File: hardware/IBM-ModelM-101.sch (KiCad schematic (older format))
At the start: 40 parts, among them J1 CONN-MOLEX-0670688000-USB-B, J2 KEYBOARD_ACTIVE_LINES, J3 KEYBOARD_INPUT_LINES, J4 CHASSIS_GROUND, J5 STATUS_LEDS, J6 DEBUG_FTDI, J7 JTAG, SW1 BOOT0, SW2 RESET, U1 TLV70233DBV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

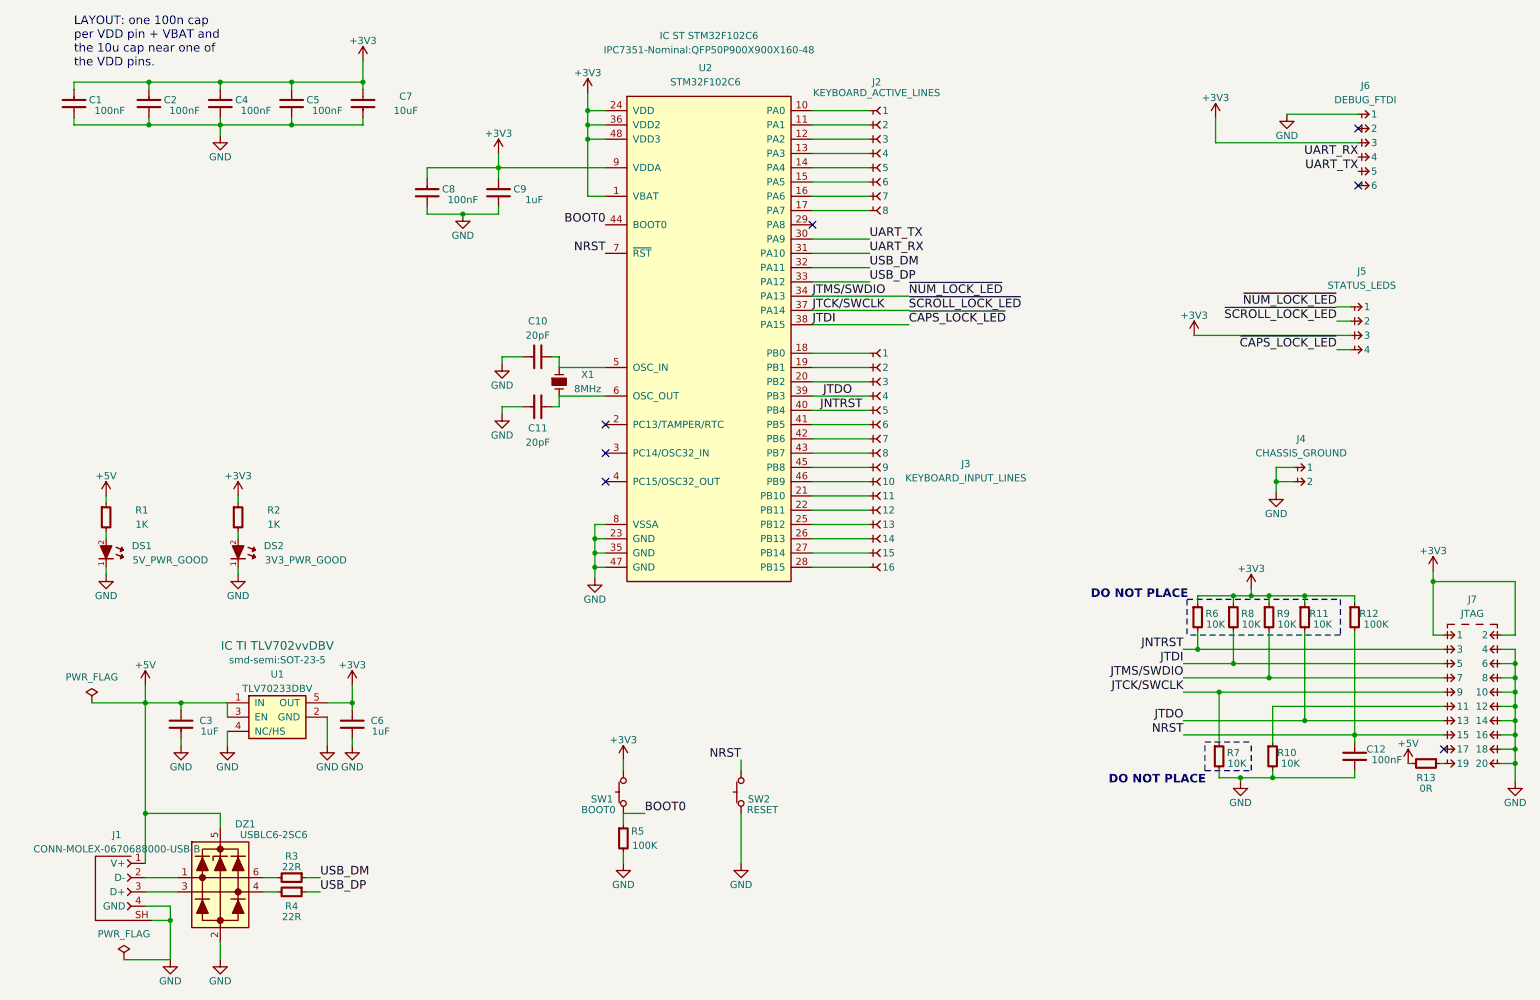
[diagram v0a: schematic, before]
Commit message: Most keys, locks working
All alpha-numerics working along with Scroll, Num andCaps lock keys.
Shift, Alt and Ctrl not working. Enter key seems to have a bug with it
as well.
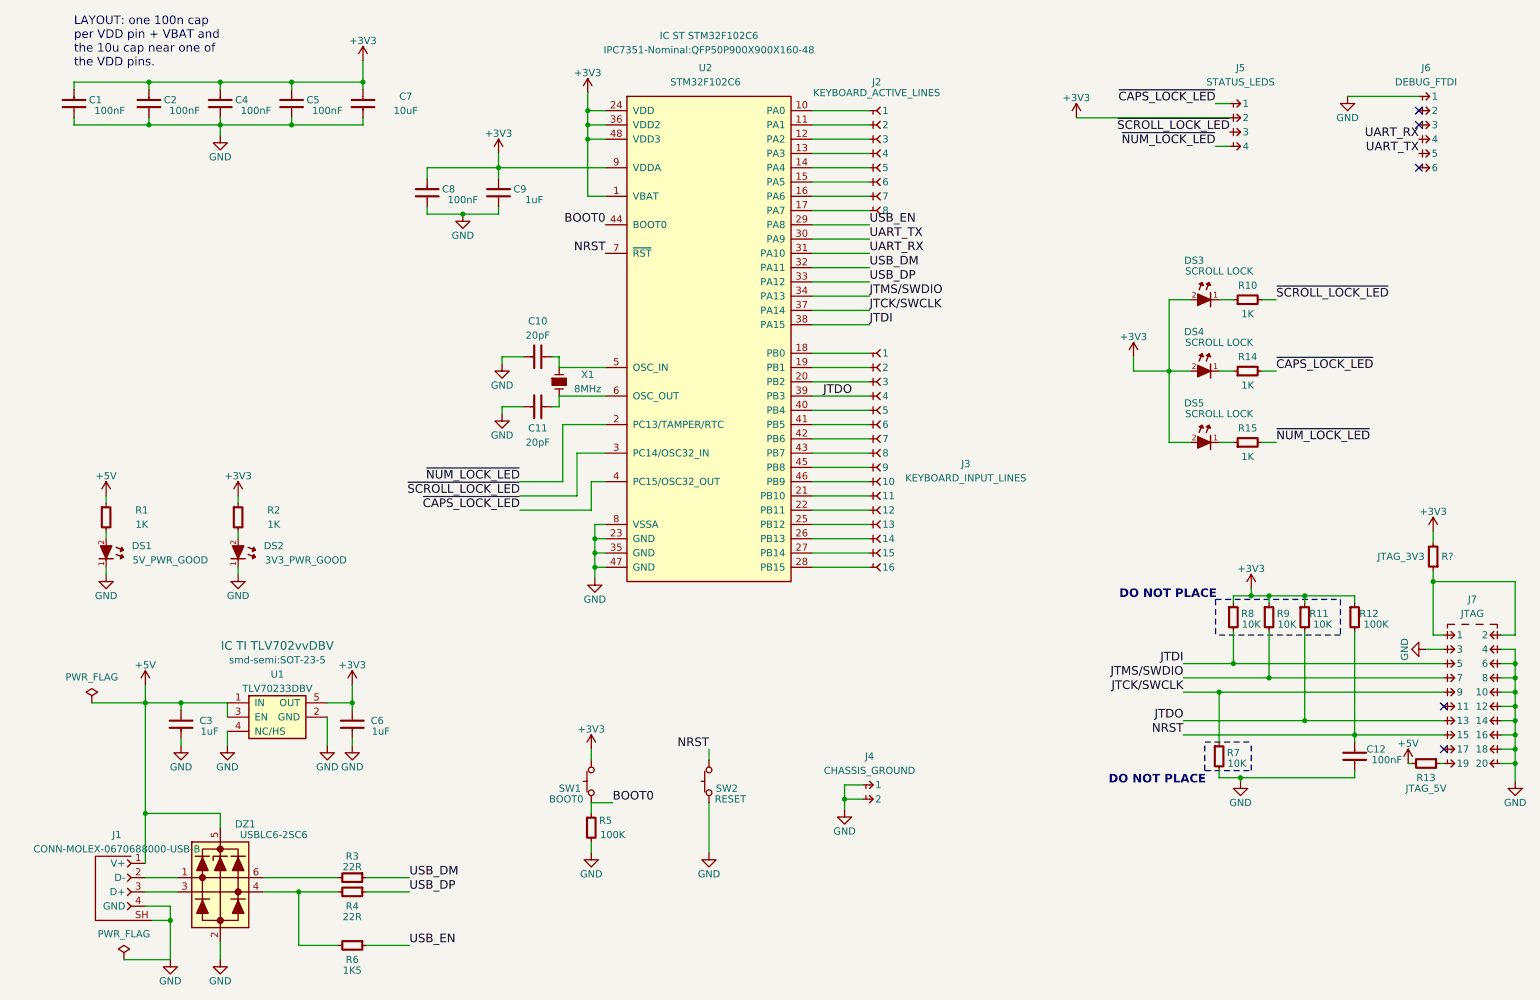
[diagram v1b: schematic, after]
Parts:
- added DS3, DS4, DS5: SCROLL LOCK, smd-semi:LED-0603, symbol LED-0603
- added R14, R15: 1K, IPC7351-Nominal:RESC1608X50, symbol R-0603
- added R?: JTAG_3V3, IPC7351-Nominal:RESC1608X50, symbol R-0603
- R10: value 10K -> 1K
- R13: value 0R -> JTAG_5V
- R6: value 10K -> 1K5
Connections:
- net +3V3: now also J5.2, DS3.2 (A), DS4.2 (A), DS5.2 (A), R?.2; no longer J5.3, J6.3, J7.1, J7.2, R6.1
- net GND: now also J7.3; no longer R10.2
- net JTCK/SWCLK: no longer J5.2
- net JTDI: no longer J5.4
- net JTMS/SWDIO: no longer J5.1
- net ~NUM_LOCK_LED~: now reaches U2.2 (PC13/TAMPER/RTC)
- net ~NUM_LOCK_LED~: now also J5.4, R15.2
- net USB_EN: now reaches U2.29 (PA8)
- net USB_EN: now also R6.1
- net ~SCROLL_LOCK_LED~: now reaches U2.3 (PC14/OSC32_IN)
- net ~SCROLL_LOCK_LED~: now also J5.3, R10.2
- net ~CAPS_LOCK_LED~: now reaches U2.4 (PC15/OSC32_OUT)
- net ~CAPS_LOCK_LED~: now also J5.1, R14.2
- net at J7.11: no longer R10.1
- net at DZ1.4, R4.2: now also R6.2
- net JNTRST: no longer names the net of J3.5, U2.40 (PB4)
- net JNTRST: no longer J7.3, R6.2
- new net: J7.1, J7.2, R?.1
- new net: DS3.1 (K), R10.1
- new net: DS5.1 (K), R15.1
- new net: DS4.1 (K), R14.1
- no-connect marks 7 -> 5
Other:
- moved on the sheet: J4, J5, J6, R3, R4, R5, SW1, SW2

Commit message: Fixed key repeat code
Keys will now stop repeating if a modifier key is released or pressed.
Key repeat will pause 500msec before turning on.
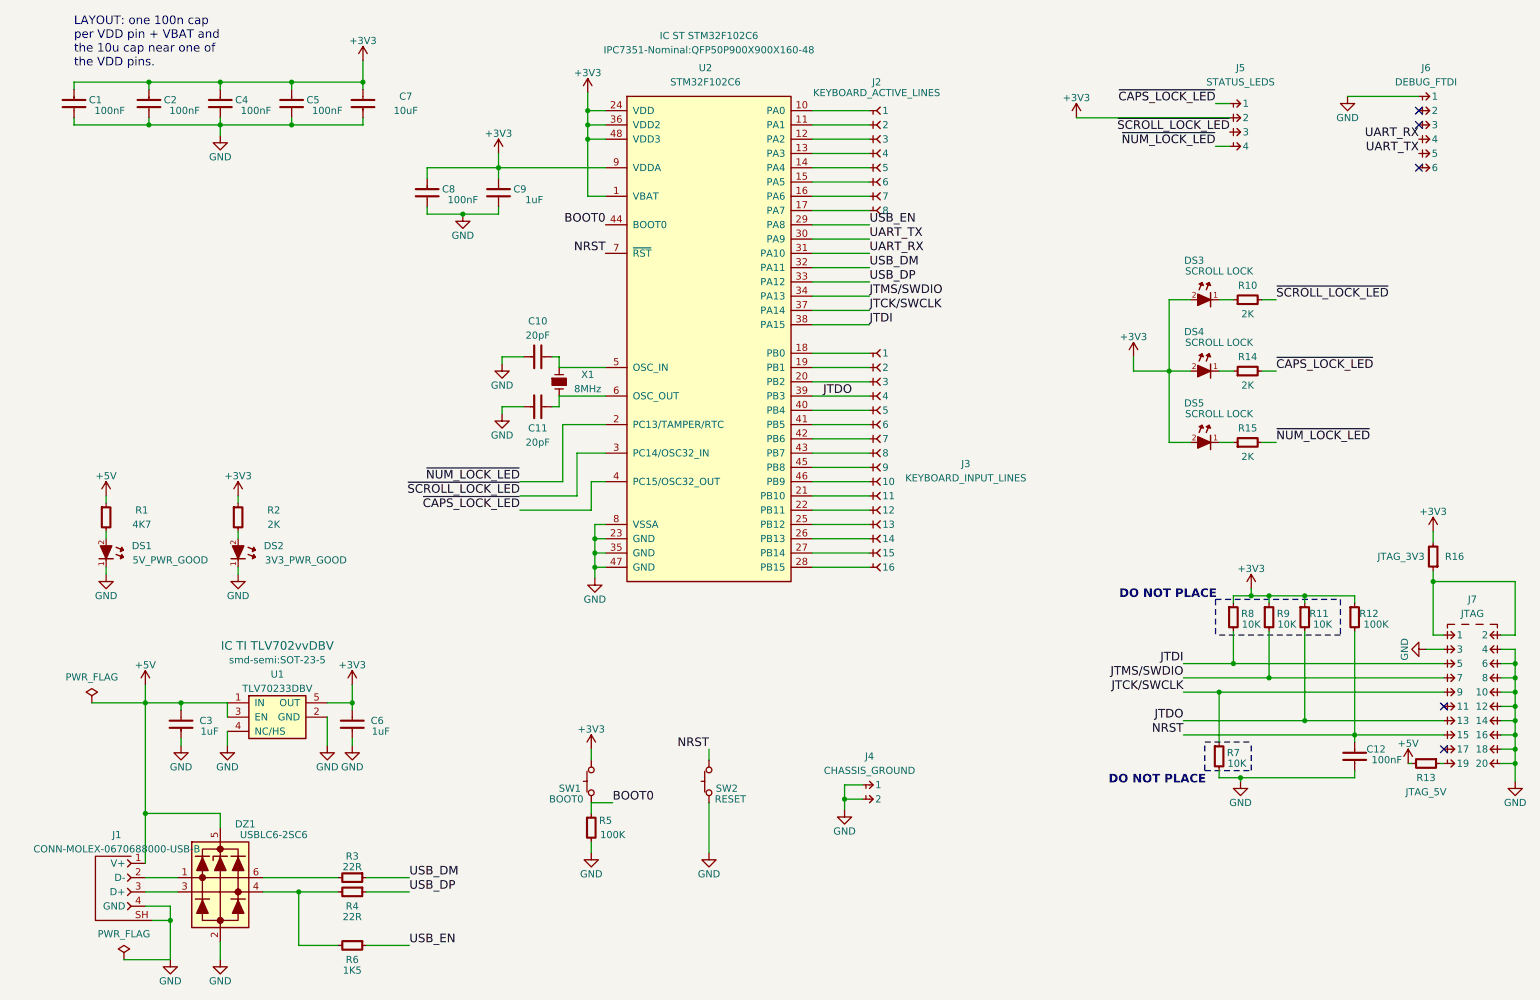
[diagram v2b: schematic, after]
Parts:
- R1: value 1K -> 4K7
- R10, R14, R15, R2: value 1K -> 2K
- gave numbers to parts that had none: 1
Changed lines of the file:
@@
 $EndComp
 $Comp
-L GND #PWR18
+L GND #PWR01
 U 1 1 573D45FD
 P 3925 3625
-F 0 "#PWR18" H 3925 3375 50  0001 C CNN
+F 0 "#PWR01" H 3925 3375 50  0001 C CNN
 F 1 "GND" H 3925 3475 50  0000 C CNN
 F 2 "" H 3925 3625 50  0000 C CNN
@@
 $EndComp
 $Comp
-L GND #PWR17
+L GND #PWR02
 U 1 1 573D462D
 P 3925 3275
-F 0 "#PWR17" H 3925 3025 50  0001 C CNN
+F 0 "#PWR02" H 3925 3025 50  0001 C CNN
 F 1 "GND" H 3925 3125 50  0000 C CNN
 F 2 "" H 3925 3275 50  0000 C CNN
@@
 $EndComp
 $Comp
-L GND #PWR13
+L GND #PWR03
 U 1 1 573D4E34
 P 2875 5950
-F 0 "#PWR13" H 2875 5700 50  0001 C CNN
+F 0 "#PWR03" H 2875 5700 50  0001 C CNN
 F 1 "GND" H 2875 5800 50  0000 C CNN
 F 2 "" H 2875 5950 50  0000 C CNN
@@
 $EndComp
 $Comp
-L GND #PWR5
+L GND #PWR04
 U 1 1 573D5176
 P 1675 5950
-F 0 "#PWR5" H 1675 5700 50  0001 C CNN
+F 0 "#PWR04" H 1675 5700 50  0001 C CNN
 F 1 "GND" H 1675 5800 50  0000 C CNN
 F 2 "" H 1675 5950 50  0000 C CNN
@@
 $EndComp
 $Comp
-L GND #PWR7
+L GND #PWR05
 U 1 1 573D535D
 P 1950 7450
-F 0 "#PWR7" H 1950 7200 50  0001 C CNN
+F 0 "#PWR05" H 1950 7200 50  0001 C CNN
 F 1 "GND" H 1950 7300 50  0000 C CNN
 F 2 "" H 1950 7450 50  0000 C CNN
@@
 $EndComp
 $Comp
-L +3V3 #PWR12
+L +3V3 #PWR06
 U 1 1 573D5F95
 P 2875 5525
-F 0 "#PWR12" H 2875 5375 50  0001 C CNN
+F 0 "#PWR06" H 2875 5375 50  0001 C CNN
 F 1 "+3V3" H 2875 5665 50  0000 C CNN
 F 2 "" H 2875 5525 50  0000 C CNN
@@
 $EndComp
 $Comp
-L GND #PWR22
+L GND #PWR07
 U 1 1 573D66DD
 P 4575 4775
-F 0 "#PWR22" H 4575 4525 50  0001 C CNN
+F 0 "#PWR07" H 4575 4525 50  0001 C CNN
 F 1 "GND" H 4575 4625 50  0000 C CNN
 F 2 "" H 4575 4775 50  0000 C CNN
@@
 $EndComp
 $Comp
-L +3V3 #PWR19
+L +3V3 #PWR08
 U 1 1 573D6AD9
 P 4525 1375
-F 0 "#PWR19" H 4525 1225 50  0001 C CNN
+F 0 "#PWR08" H 4525 1225 50  0001 C CNN
 F 1 "+3V3" H 4525 1515 50  0000 C CNN
 F 2 "" H 4525 1375 50  0000 C CNN
@@
 USB_DP
 $Comp
-L GND #PWR33
+L GND #PWR09
 U 1 1 573DD1DD
 P 11025 6200
-F 0 "#PWR33" H 11025 5950 50  0001 C CNN
+F 0 "#PWR09" H 11025 5950 50  0001 C CNN
 F 1 "GND" H 11025 6050 50  0000 C CNN
 F 2 "" H 11025 6200 50  0000 C CNN
@@
 $EndComp
 $Comp
-L +3V3 #PWR32
+L +3V3 #PWR010
 U 1 1 573DDDD0
 P 10450 4450
-F 0 "#PWR32" H 10450 4300 50  0001 C CNN
+F 0 "#PWR010" H 10450 4300 50  0001 C CNN
 F 1 "+3V3" H 10450 4590 50  0000 C CNN
 F 2 "" H 10450 4450 50  0000 C CNN
@@
 $EndComp
 $Comp
-L GND #PWR27
+L GND #PWR011
 U 1 1 573E00B2
 P 9100 6200
-F 0 "#PWR27" H 9100 5950 50  0001 C CNN
+F 0 "#PWR011" H 9100 5950 50  0001 C CNN
 F 1 "GND" H 9100 6050 50  0000 C CNN
 F 2 "" H 9100 6200 50  0000 C CNN
@@
 $EndComp
 $Comp
-L +3V3 #PWR28
+L +3V3 #PWR012
 U 1 1 573E0DF0
 P 9175 4850
-F 0 "#PWR28" H 9175 4700 50  0001 C CNN
+F 0 "#PWR012" H 9175 4700 50  0001 C CNN
 F 1 "+3V3" H 9175 4990 50  0000 C CNN
 F 2 "" H 9175 4850 50  0000 C CNN
@@
 NRST
 $Comp
-L +5V #PWR3
+L +5V #PWR013
 U 1 1 573E26F3
 P 1425 5525
-F 0 "#PWR3" H 1425 5375 50  0001 C CNN
+F 0 "#PWR013" H 1425 5375 50  0001 C CNN
 F 1 "+5V" H 1425 5665 50  0000 C CNN
 F 2 "" H 1425 5525 50  0000 C CNN
@@
 $EndComp
 $Comp
-L +5V #PWR30
+L +5V #PWR014
 U 1 1 573E2E47
 P 10275 6075
-F 0 "#PWR30" H 10275 5925 50  0001 C CNN
+F 0 "#PWR014" H 10275 5925 50  0001 C CNN
 F 1 "+5V" H 10275 6215 50  0000 C CNN
 F 2 "" H 10275 6075 50  0000 C CNN
@@
 P 10400 6075
 F 0 "R13" V 10500 6075 50  0000 C CNN
-F 1 "JTAG_5V" V 10575 6075 50  0000 C CNN
+F 1 "JTAG_5V" V 10600 6075 50  0000 C CNN
 F 2 "IPC7351-Nominal:RESC1608X50" H 10400 6075 50  0001 C CNN
 F 3 "" H 10400 6125 60  0000 C CNN
@@
 $EndComp
 $Comp
-L GND #PWR6
+L GND #PWR015
 U 1 1 573DF32C
 P 1950 1675
-F 0 "#PWR6" H 1950 1425 50  0001 C CNN
+F 0 "#PWR015" H 1950 1425 50  0001 C CNN
 F 1 "GND" H 1950 1525 50  0000 C CNN
 F 2 "" H 1950 1675 50  0000 C CNN
@@
 $EndComp
 $Comp
-L GND #PWR21
+L GND #PWR016
 U 1 1 573E1C4C
 P 4550 6700
-F 0 "#PWR21" H 4550 6450 50  0001 C CNN
+F 0 "#PWR016" H 4550 6450 50  0001 C CNN
 F 1 "GND" H 4550 6550 50  0000 C CNN
 F 2 "" H 4550 6700 50  0000 C CNN
@@
 BOOT0
 $Comp
-L +3V3 #PWR20
+L +3V3 #PWR017
 U 1 1 573E27FC
 P 4550 5975
-F 0 "#PWR20" H 4550 5825 50  0001 C CNN
+F 0 "#PWR017" H 4550 5825 50  0001 C CNN
 F 1 "+3V3" H 4550 6115 50  0000 C CNN
 F 2 "" H 4550 5975 50  0000 C CNN
@@
 BOOT0
 $Comp
-L +3V3 #PWR16
+L +3V3 #PWR018
 U 1 1 573E49A4
 P 3900 1800
-F 0 "#PWR16" H 3900 1650 50  0001 C CNN
+F 0 "#PWR018" H 3900 1650 50  0001 C CNN
 F 1 "+3V3" H 3900 1940 50  0000 C CNN
 F 2 "" H 3900 1800 50  0000 C CNN
@@
 $EndComp
 $Comp
-L GND #PWR15
+L GND #PWR019
 U 1 1 573E51BE
 P 3650 2225
-F 0 "#PWR15" H 3650 1975 50  0001 C CNN
+F 0 "#PWR019" H 3650 1975 50  0001 C CNN
 F 1 "GND" H 3650 2075 50  0000 C CNN
 F 2 "" H 3650 2225 50  0000 C CNN
@@
 NRST
 $Comp
-L GND #PWR23
+L GND #PWR020
 U 1 1 573E7827
 P 5375 6700
-F 0 "#PWR23" H 5375 6450 50  0001 C CNN
+F 0 "#PWR020" H 5375 6450 50  0001 C CNN
 F 1 "GND" H 5375 6550 50  0000 C CNN
 F 2 "" H 5375 6700 50  0000 C CNN
@@
 ~CAPS_LOCK_LED~
 $Comp
-L +3V3 #PWR14
+L +3V3 #PWR021
 U 1 1 57424B72
 P 2950 1150
-F 0 "#PWR14" H 2950 1000 50  0001 C CNN
+F 0 "#PWR021" H 2950 1000 50  0001 C CNN
 F 1 "+3V3" H 2950 1290 50  0000 C CNN
 F 2 "" H 2950 1150 50  0000 C CNN
@@
 $EndComp
 $Comp
-L GND #PWR11
+L GND #PWR022
 U 1 1 57428CE5
 P 2700 5950
-F 0 "#PWR11" H 2700 5700 50  0001 C CNN
+F 0 "#PWR022" H 2700 5700 50  0001 C CNN
 F 1 "GND" H 2700 5800 50  0000 C CNN
 F 2 "" H 2700 5950 50  0000 C CNN
@@
 $EndComp
 $Comp
-L GND #PWR4
+L GND #PWR023
 U 1 1 5742A162
 P 1600 7450
-F 0 "#PWR4" H 1600 7200 50  0001 C CNN
+F 0 "#PWR023" H 1600 7200 50  0001 C CNN
 F 1 "GND" H 1600 7300 50  0000 C CNN
 F 2 "" H 1600 7450 50  0000 C CNN
@@
 $EndComp
 $Comp
-L GND #PWR29
+L GND #PWR024
 U 1 1 5742C722
 P 9850 1400
-F 0 "#PWR29" H 9850 1150 50  0001 C CNN
+F 0 "#PWR024" H 9850 1150 50  0001 C CNN
 F 1 "GND" H 9850 1250 50  0000 C CNN
 F 2 "" H 9850 1400 50  0000 C CNN
@@
 UART_RX
 $Comp
-L PWR_FLAG #FLG1
+L PWR_FLAG #FLG025
 U 1 1 57430659
 P 1050 5650
-F 0 "#FLG1" H 1050 5745 50  0001 C CNN
+F 0 "#FLG025" H 1050 5745 50  0001 C CNN
 F 1 "PWR_FLAG" H 1050 5830 50  0000 C CNN
 F 2 "" H 1050 5650 50  0000 C CNN
@@
 $EndComp
 $Comp
-L PWR_FLAG #FLG2
+L PWR_FLAG #FLG026
 U 1 1 574315A9
 P 1275 7450
-F 0 "#FLG2" H 1275 7545 50  0001 C CNN
+F 0 "#FLG026" H 1275 7545 50  0001 C CNN
 F 1 "PWR_FLAG" H 1275 7630 50  0000 C CNN
 F 2 "" H 1275 7450 50  0000 C CNN
@@
 $EndComp
 $Comp
-L GND #PWR24
+L GND #PWR027
 U 1 1 57433FE0
 P 6325 6400
-F 0 "#PWR24" H 6325 6150 50  0001 C CNN
+F 0 "#PWR027" H 6325 6150 50  0001 C CNN
 F 1 "GND" H 6325 6250 50  0000 C CNN
 F 2 "" H 6325 6400 50  0000 C CNN
@@
 $EndComp
 $Comp
-L +5V #PWR1
+L +5V #PWR028
 U 1 1 5743BD79
 P 1150 4200
-F 0 "#PWR1" H 1150 4050 50  0001 C CNN
+F 0 "#PWR028" H 1150 4050 50  0001 C CNN
 F 1 "+5V" H 1150 4340 50  0000 C CNN
 F 2 "" H 1150 4200 50  0000 C CNN
@@
 $EndComp
 $Comp
-L +3V3 #PWR9
+L +3V3 #PWR029
 U 1 1 5743BDF0
 P 2075 4200
-F 0 "#PWR9" H 2075 4050 50  0001 C CNN
+F 0 "#PWR029" H 2075 4050 50  0001 C CNN
 F 1 "+3V3" H 2075 4340 50  0000 C CNN
 F 2 "" H 2075 4200 50  0000 C CNN
@@
 $EndComp
 $Comp
-L GND #PWR2
+L GND #PWR030
 U 1 1 5743BE67
 P 1150 4750
-F 0 "#PWR2" H 1150 4500 50  0001 C CNN
+F 0 "#PWR030" H 1150 4500 50  0001 C CNN
 F 1 "GND" H 1150 4600 50  0000 C CNN
 F 2 "" H 1150 4750 50  0000 C CNN
@@
 $EndComp
 $Comp
-L GND #PWR10
+L GND #PWR031
 U 1 1 5743BEDE
 P 2075 4750
-F 0 "#PWR10" H 2075 4500 50  0001 C CNN
+F 0 "#PWR031" H 2075 4500 50  0001 C CNN
 F 1 "GND" H 2075 4600 50  0000 C CNN
 F 2 "" H 2075 4750 50  0000 C CNN
@@
 P 1150 4350
 F 0 "R1" H 1400 4400 50  0000 C CNN
-F 1 "1K" H 1400 4300 50  0000 C CNN
+F 1 "4K7" H 1400 4300 50  0000 C CNN
 F 2 "IPC7351-Nominal:RESC1608X50" H 1150 4350 50  0001 C CNN
 F 3 "" H 1150 4400 60  0000 C CNN
@@
 P 2075 4350
 F 0 "R2" H 2325 4400 50  0000 C CNN
-F 1 "1K" H 2325 4300 50  0000 C CNN
+F 1 "2K" H 2325 4300 50  0000 C CNN
 F 2 "IPC7351-Nominal:RESC1608X50" H 2075 4350 50  0001 C CNN
 F 3 "" H 2075 4400 60  0000 C CNN
@@
 $EndComp
 $Comp
-L GND #PWR8
+L GND #PWR032
 U 1 1 5743B0ED
 P 2000 5950
-F 0 "#PWR8" H 2000 5700 50  0001 C CNN
+F 0 "#PWR032" H 2000 5700 50  0001 C CNN
 F 1 "GND" H 2000 5800 50  0000 C CNN
 F 2 "" H 2000 5950 50  0000 C CNN
@@
 	9050 4900 9900 4900
 $Comp
-L GND #PWR31
+L GND #PWR033
 U 1 1 57B04156
 P 10400 5275
-F 0 "#PWR31" H 10400 5025 50  0001 C CNN
+F 0 "#PWR033" H 10400 5025 50  0001 C CNN
 F 1 "GND" H 10400 5125 50  0000 C CNN
 F 2 "" H 10400 5275 50  0000 C CNN
@@
 P 9150 2825
 F 0 "R10" V 9250 2825 50  0000 C CNN
-F 1 "1K" V 9050 2825 50  0000 C CNN
+F 1 "2K" V 9050 2825 50  0000 C CNN
 F 2 "IPC7351-Nominal:RESC1608X50" H 9150 2825 50  0001 C CNN
 F 3 "" H 9150 2875 60  0000 C CNN
@@
 P 9150 3325
 F 0 "R14" V 9250 3325 50  0000 C CNN
-F 1 "1K" V 9050 3325 50  0000 C CNN
+F 1 "2K" V 9050 3325 50  0000 C CNN
 F 2 "IPC7351-Nominal:RESC1608X50" H 9150 3325 50  0001 C CNN
 F 3 "" H 9150 3375 60  0000 C CNN
@@
 P 9150 3825
 F 0 "R15" V 9250 3825 50  0000 C CNN
-F 1 "1K" V 9050 3825 50  0000 C CNN
+F 1 "2K" V 9050 3825 50  0000 C CNN
 F 2 "IPC7351-Nominal:RESC1608X50" H 9150 3825 50  0001 C CNN
 F 3 "" H 9150 3875 60  0000 C CNN
@@
 ~NUM_LOCK_LED~
 $Comp
-L +3V3 #PWR26
+L +3V3 #PWR034
 U 1 1 57B0D230
 P 8350 3225
-F 0 "#PWR26" H 8350 3075 50  0001 C CNN
+F 0 "#PWR034" H 8350 3075 50  0001 C CNN
 F 1 "+3V3" H 8350 3365 50  0000 C CNN
 F 2 "" H 8350 3225 50  0000 C CNN
@@
 	8950 3825 9050 3825
 $Comp
-L R-0603 R?
+L R-0603 R16
 U 1 1 57B1046C
 P 10450 4625
-F 0 "R?" H 10350 4625 50  0000 C CNN
+F 0 "R16" H 10300 4625 50  0000 C CNN
 F 1 "JTAG_3V3" H 10675 4625 50  0000 C CNN
 F 2 "IPC7351-Nominal:RESC1608X50" H 10450 4625 50  0001 C CNN
@@
 	10450 4450 10450 4525
 $Comp
-L +3V3 #PWR25
+L +3V3 #PWR035
 U 1 1 5742D533
 P 7950 1550
-F 0 "#PWR25" H 7950 1400 50  0001 C CNN
+F 0 "#PWR035" H 7950 1400 50  0001 C CNN
 F 1 "+3V3" H 7950 1690 50  0000 C CNN
 F 2 "" H 7950 1550 50  0000 C CNN
